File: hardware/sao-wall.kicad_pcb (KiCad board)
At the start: 2 copper layers, 320 x 30 mm, 37 parts, among them CON1 AVR-ISP-6, J1 PMOD-2x6-MALE, J2 PMOD-2x6-FEMALE, Q1 AO3401A, Q2 AO3401A, U1 ATmega32U4-MU, U2 TLV62569DBVR, X1 16MHz, X2 A, X3 B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

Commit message: hardware: Nov2020 version of pcb with errata fixed
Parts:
- removed C15, C5, C7: 10uF/6.3V, tom-passives:C_0805_2012Metric
- added Q3: PMBT2907A_PNP_500mA, tom-semiconductors:SOT23_NXP, B.Cu at (189.0, 11.0)
- added R8: 1k, tom-passives:R_0805_2012Metric, B.Cu at (108.0, 10.0)
- added TCK1: TCK, tom-mechanical:TestPoint_Pad_D1.5mm, B.Cu at (181.6, 11.0)
- added TDI1: TDI, tom-mechanical:TestPoint_Pad_D1.5mm, B.Cu at (174.0, 11.0)
- added TDO1: TDO, tom-mechanical:TestPoint_Pad_D1.5mm, B.Cu at (176.5, 11.0)
- added TMS1: TMS, tom-mechanical:TestPoint_Pad_D1.5mm, B.Cu at (179.1, 11.0)
- CON1: footprint tom-connectors:PinSocket_2x03_P2.54mm_Vertical_SMD_SAO -> tom-connectors:PinTestpoint_2x03_P2.54mm_Vertical
- Q1, Q2: value AO3401A -> PMBT2907A_PNP_500mA; footprint tom-semiconductors:SOT-23 -> tom-semiconductors:SOT23_NXP
- R1: value 10k -> 1k
- TP1: footprint tom-mechanical:TestPoint_Pad_D3.0mm -> tom-mechanical:TestPoint_Pad_D1.5mm
- moved C6 160.0 mm to (274.0, 15.0)
- moved Q2 77.0 mm to (113.0, 11.0), turned to 0 degrees
- moved C8 9.11 mm to (26.1, 15.0)
- moved R2 8.00 mm to (185.0, 10.0), turned to 0 degrees
- moved R1 5.10 mm to (32.0, 15.0), turned to 90 degrees
- moved Q1 3.61 mm to (33.0, 11.0), turned to 0 degrees
- moved CON1 2.72 mm to (153.2, 22.3)
- moved J1 2.00 mm to (311.0, 15.0)
- moved J2 2.00 mm to (14.0, 15.0)
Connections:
- Q1 pad 1: /A_PWM -> Net-(Q1-Pad1)
- Q1 pad 2: /A_VCC -> +3V3
- Q1 pad 3: +3V3 -> /A_VCC
- Q2 pad 1: /C_PWM -> Net-(Q2-Pad1)
- Q2 pad 2: /C_VCC -> +3V3
- Q2 pad 3: +3V3 -> /B_VCC
- R1 pad 1: +3V3 -> /A_PWM
- R1 pad 2: /A_PWM -> Net-(Q1-Pad1)
- R2 pad 1: +3V3 -> /C_PWM
- R2 pad 2: /C_PWM -> Net-(Q3-Pad1)
- U1 pad 22: Net-(U1-Pad22) -> /C_GPIO1
- U1 pad 25: Net-(U1-Pad25) -> /C_GPIO2
- U1 pad 31: /B_GPIO1 -> /B_PWM
- U1 pad 36: Net-(U1-Pad36) -> /TDI
- U1 pad 37: Net-(U1-Pad37) -> /TDO
- U1 pad 38: /C_GPIO1 -> /TMS
- U1 pad 39: /C_GPIO2 -> /TCK
- U1 pad 8: Net-(U1-Pad8) -> /B_GPIO1
- X3 pad 1: +3V3 -> /B_VCC
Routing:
- net /B_PWM: track 0.00 -> 67.9 mm, vias 0 -> 2
- net /TCK: track 0.00 -> 20.6 mm, vias 0 -> 2
- net /C_GPIO1: track 41.9 -> 62.2 mm, vias 0 -> 2
- net +3V3: track 380.4 -> 399.5 mm, vias 3 -> 4
- net /TMS: track 0.00 -> 17.4 mm
- net /TDO: track 0.00 -> 14.3 mm
- net /MISO: track 18.1 -> 5.94 mm, vias 2 -> 1
- net /C_GPIO2: track 42.3 -> 54.4 mm, vias 0 -> 2
- net /TDI: track 0.00 -> 11.6 mm
- net /C_PWM: track 36.6 -> 25.9 mm
- net /SCK: track 15.0 -> 5.02 mm, vias 0 -> 1
- net +5V: track 448.0 -> 442.3 mm, vias 8 -> 7
- net /A_PWM: track 133.7 -> 128.3 mm
- net /B_VCC: track 0.00 -> 5.40 mm
- net Net-(Q1-Pad1): track 0.00 -> 4.03 mm
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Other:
- rule pad_to_mask_clearance: 0.05 -> 0
- board text added: "sao-wall tom@tomk.in Nov2020"
- board text removed: "sao-wall tom@tomk.in Sep2020"

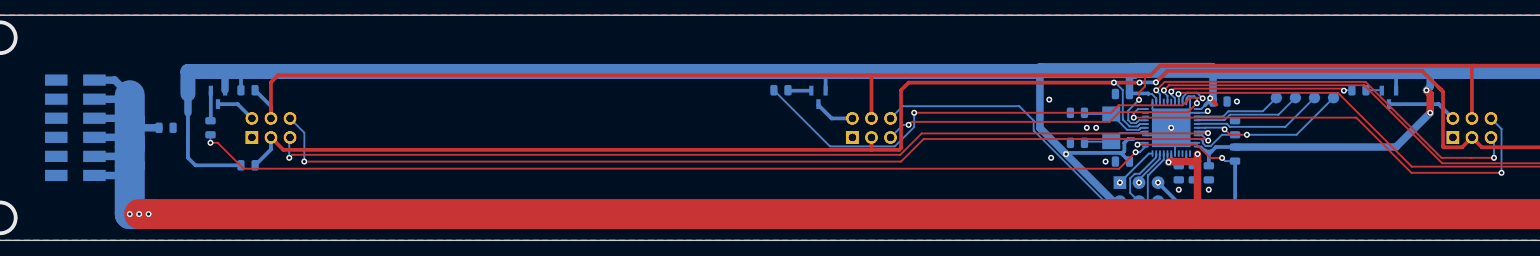
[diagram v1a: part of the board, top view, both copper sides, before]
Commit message: hardware: move to QFP cpu package, Dec2022 release
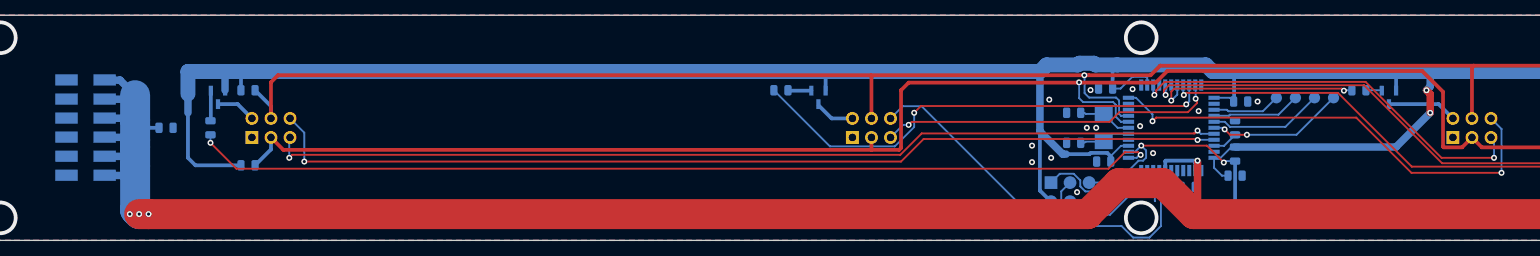
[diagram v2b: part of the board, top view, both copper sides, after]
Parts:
- U1: footprint tom-semiconductors:QFN-44-1EP_7x7mm_P0.5mm_EP5.15x5.15mm -> tom-semiconductors:TQFP-44_10x10mm_P0.8mm
- moved CON1 9.19 mm to (144.0, 22.3)
- moved C12 3.52 mm to (168.5, 21.4), turned to 0 degrees
- moved C4 2.93 mm to (158.8, 22.9), turned to 180 degrees
- moved C11 2.75 mm to (169.2, 11.5)
- moved C10 2.50 mm to (151.0, 19.5)
- moved C16 2.36 mm to (151.2, 9.78)
- moved C9 2.02 mm to (162.2, 22.9), turned to 180 degrees
- moved J2 1.36 mm to (15.4, 15.0)
- moved X1 1.00 mm to (151.0, 15.0)
- moved C1 0.50 mm to (147.0, 13.0)
- moved C2 0.50 mm to (147.0, 17.0)
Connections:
- net +3V3 renamed +3.3V
- U1 pad 1: Net-(U1-Pad1) -> unconnected-(U1-Pad1)
- U1 pad 20: Net-(U1-Pad20) -> unconnected-(U1-Pad20)
- U1 pad 21: Net-(U1-Pad21) -> unconnected-(U1-Pad21)
- U1 pad 26: Net-(U1-Pad26) -> unconnected-(U1-Pad26)
- U1 pad 28: Net-(U1-Pad28) -> unconnected-(U1-Pad28)
- U1 pad 3: Net-(U1-Pad3) -> unconnected-(U1-Pad3)
- U1 pad 4: Net-(U1-Pad4) -> unconnected-(U1-Pad4)
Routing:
- net GND: track 26.5 -> 4.30 mm, vias 14 -> 19
- net /SCK: track 5.02 -> 19.2 mm, vias 1 -> 0
- net /MISO: track 5.94 -> 15.1 mm, vias 1 -> 0
- net /MOSI: track 8.72 -> 13.6 mm
- net /B_PWM: track 67.9 -> 64.2 mm
- net +5V: track 442.3 -> 445.3 mm, vias 7 -> 6
- net /AREF: track 6.23 -> 3.41 mm
- net +3.3V: track 399.5 -> 396.7 mm, vias 4 -> 2
- net /TDO: track 14.3 -> 11.8 mm
- net /B_GPIO1: track 49.6 -> 52.1 mm
- net /TDI: track 11.6 -> 9.13 mm
- net /TCK: track 20.6 -> 18.3 mm
- net /TMS: track 17.4 -> 15.3 mm
- net /C_PWM: track 25.9 -> 28.0 mm
- net /XTAL1: track 9.18 -> 7.69 mm
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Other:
- net class Default removed
- board text added: "sao-wall tom@tomk.in Dec2022"
- board text removed: "sao-wall tom@tomk.in Nov2020"
